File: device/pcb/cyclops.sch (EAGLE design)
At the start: 180 parts, among them Q1 SSM3K324, Q2 SSM3K324, Q3 SSM3K324, Q4 IRF510, U1 MCP4921, U10 ADG1202, U11 THS4281, U12 MAX4564, U13 ZXTD, U14 ZXTD, U15 OPA1664, U2 LT1931, U3 LT1764A, U31 TPS62153, U4 BD00FC0WEFJ, U5 TPS72325, U6 LT1711, U7 TLV3701, U8 ADR03, U9 LT1880

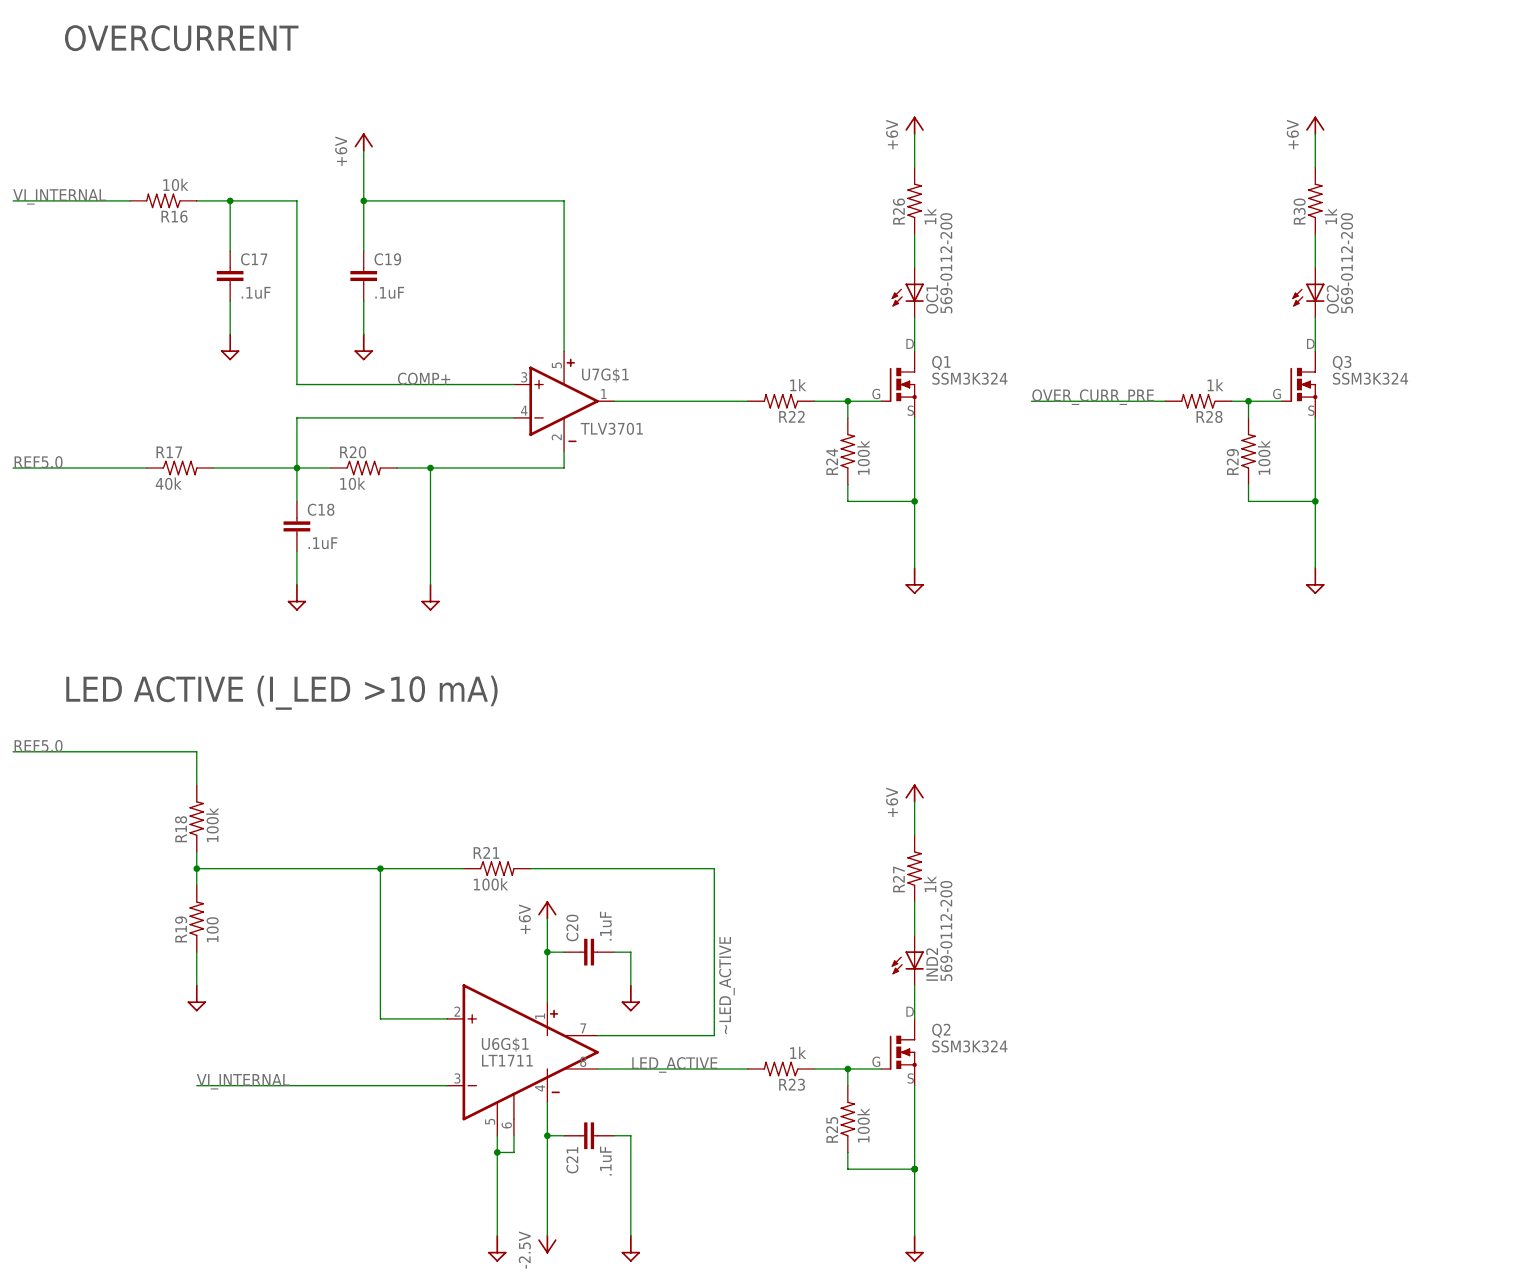
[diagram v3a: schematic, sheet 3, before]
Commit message: Minor circuit changes made during testing.
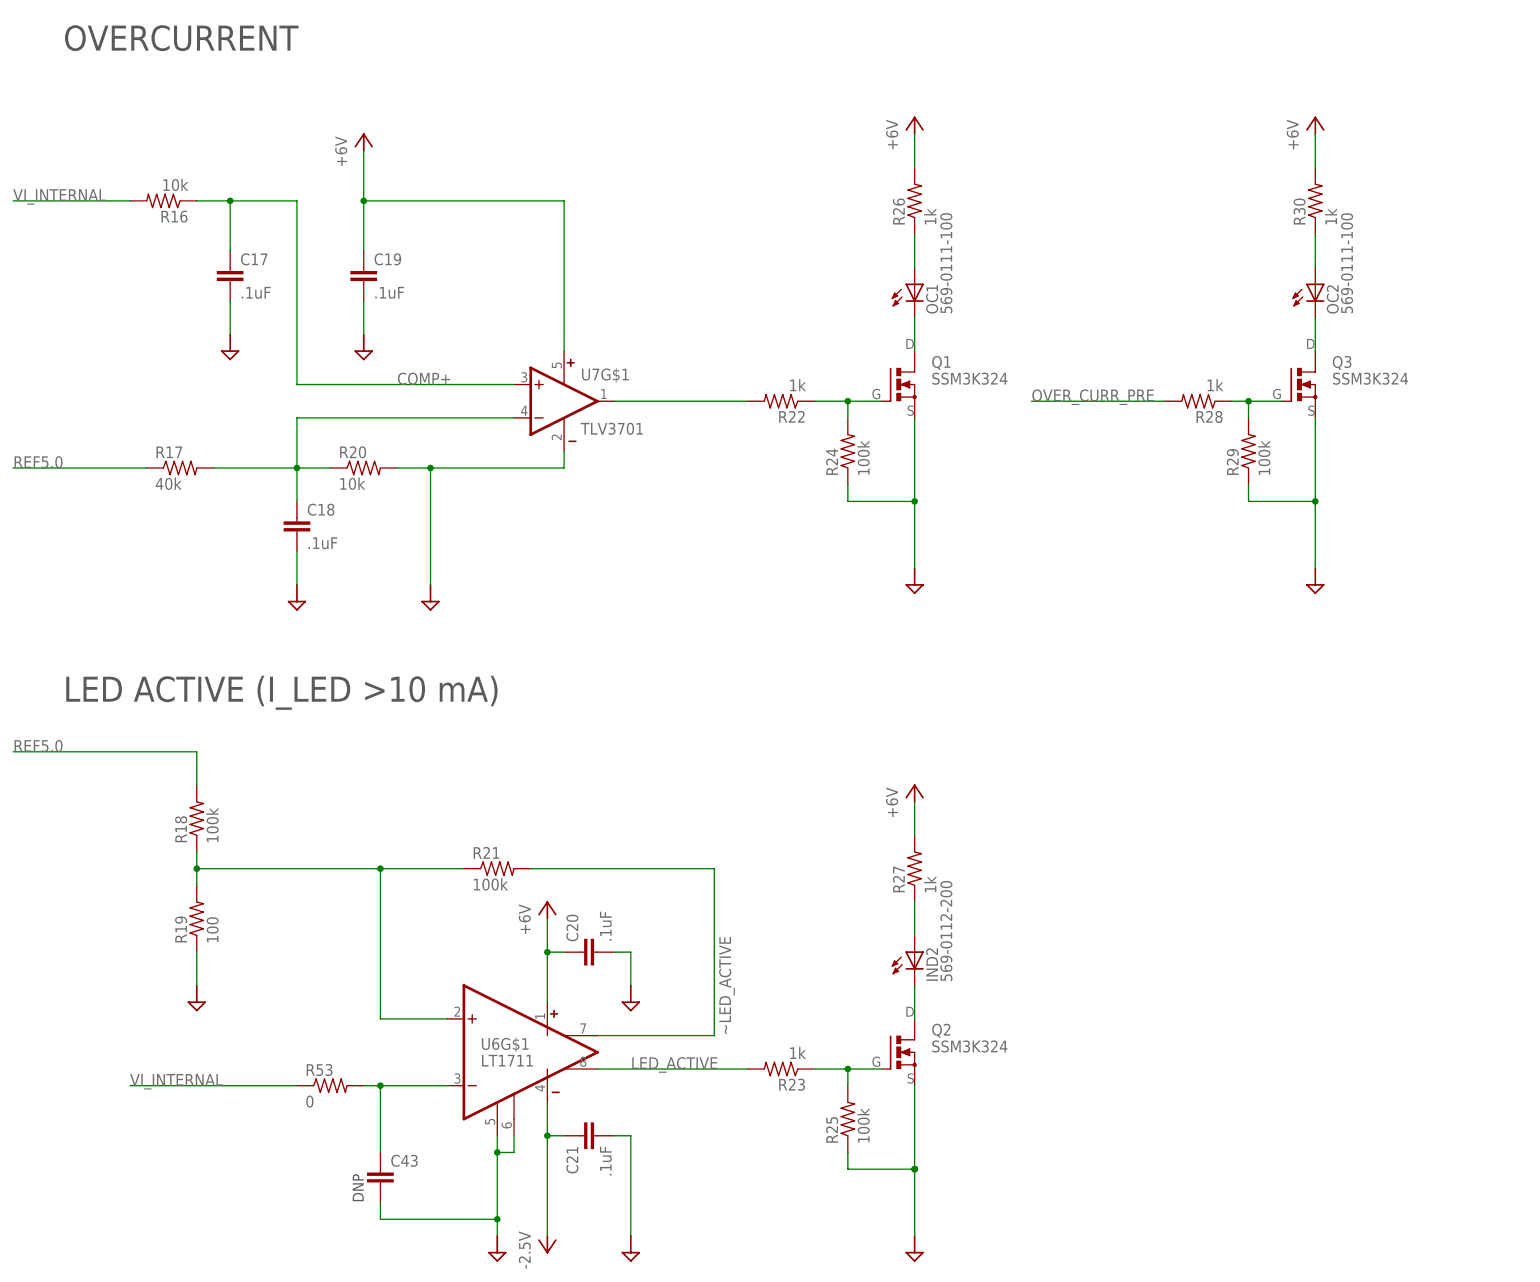
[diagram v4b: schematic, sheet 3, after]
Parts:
- added C43: (no value), cyclops:C_0603
- added R53: 0, cyclops:R_0603
- OC: value 569-0112-200 -> 569-0111-100
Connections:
- new net N$7: C43.1, R53.2, U6G$1.-IN
- net GND: now also C43.2
- net VI_INTERNAL: now also R53.1; no longer U6G$1.-IN
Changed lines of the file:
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@@
 <part name="R37" library="cyclops" deviceset="R" device="_0603" value="0"/>
 <part name="IND" library="jonnew" deviceset="LED_2X" device="_VERTICAL" value="569-0112-200"/>
-<part name="OC" library="jonnew" deviceset="LED_2X" device="_VERTICAL" value="569-0112-200"/>
+<part name="OC" library="jonnew" deviceset="LED_2X" device="_VERTICAL" value="569-0111-100"/>
 <part name="D2" library="jonnew" deviceset="S-DIODE" device="SOD-123" value="1N5819"/>
 <part name="VREF&lt;&gt;TTL" library="jonnew" deviceset="SPDT" device="_AS12A*" value="AS12CV"/>
@@
 <part name="U$80" library="jonnew" deviceset="TEENSY-2-PIN-HEADER" device="" value="PPPC021LFBN-RC"/>
 <part name="P+20" library="cyclops" deviceset="+5V" device="" value="+3V3"/>
+<part name="C43" library="cyclops" deviceset="C" device="_0603"/>
+<part name="R53" library="cyclops" deviceset="R" device="_0603" value="0"/>
 </parts>
 <sheets>
@@
 <text x="-109.22" y="22.86" size="3.81" layer="97">LED ACTIVE (I_LED &gt;10 mA)</text>
 <text x="-109.22" y="121.92" size="3.81" layer="97">OVERCURRENT</text>
+<text x="-63.5" y="-53.34" size="1.6764" layer="97" rot="R90">DNP</text>
 </plain>
 <instances>
@@
 <instance part="P+11" gate="1" x="20.32" y="10.16"/>
 <instance part="P+14" gate="1" x="-63.5" y="109.22"/>
+<instance part="C43" gate="C" x="-60.96" y="-48.26"/>
+<instance part="R53" gate="R" x="-68.58" y="-35.56" smashed="yes">
+<attribute name="NAME" x="-72.39" y="-34.0614" size="1.778" layer="95"/>
+<attribute name="VALUE" x="-72.39" y="-38.862" size="1.778" layer="96"/>
+</instance>
 </instances>
 <busses>
@@
 <wire x1="-43.18" y1="-45.72" x2="-43.18" y2="-43.18" width="0.1524" layer="91"/>
 <junction x="-43.18" y="-45.72"/>
-<wire x1="-43.18" y1="-45.72" x2="-43.18" y2="-58.42" width="0.1524" layer="91"/>
+<wire x1="-43.18" y1="-45.72" x2="-43.18" y2="-55.88" width="0.1524" layer="91"/>
+<pinref part="C43" gate="C" pin="2"/>
+<wire x1="-43.18" y1="-55.88" x2="-43.18" y2="-58.42" width="0.1524" layer="91"/>
+<wire x1="-60.96" y1="-53.34" x2="-60.96" y2="-55.88" width="0.1524" layer="91"/>
+<wire x1="-60.96" y1="-55.88" x2="-43.18" y2="-55.88" width="0.1524" layer="91"/>
+<junction x="-43.18" y="-55.88"/>
 </segment>
 <segment>
@@
 </segment>
 <segment>
-<label x="-88.9" y="-35.56" size="1.778" layer="95"/>
-<wire x1="-88.9" y1="-35.56" x2="-50.8" y2="-35.56" width="0.1524" layer="91"/>
-<pinref part="U6" gate="G$1" pin="-IN"/>
+<label x="-99.06" y="-35.56" size="1.778" layer="95"/>
+<pinref part="R53" gate="R" pin="1"/>
+<wire x1="-73.66" y1="-35.56" x2="-99.06" y2="-35.56" width="0.1524" layer="91"/>
 </segment>
 </net>
@@
 </segment>
 </net>
+<net name="N$7" class="0">
+<segment>
+<pinref part="R53" gate="R" pin="2"/>
+<pinref part="C43" gate="C" pin="1"/>
+<wire x1="-63.5" y1="-35.56" x2="-60.96" y2="-35.56" width="0.1524" layer="91"/>
+<wire x1="-60.96" y1="-35.56" x2="-60.96" y2="-45.72" width="0.1524" layer="91"/>
+<pinref part="U6" gate="G$1" pin="-IN"/>
+<wire x1="-60.96" y1="-35.56" x2="-50.8" y2="-35.56" width="0.1524" layer="91"/>
+<junction x="-60.96" y="-35.56"/>
+</segment>
+</net>

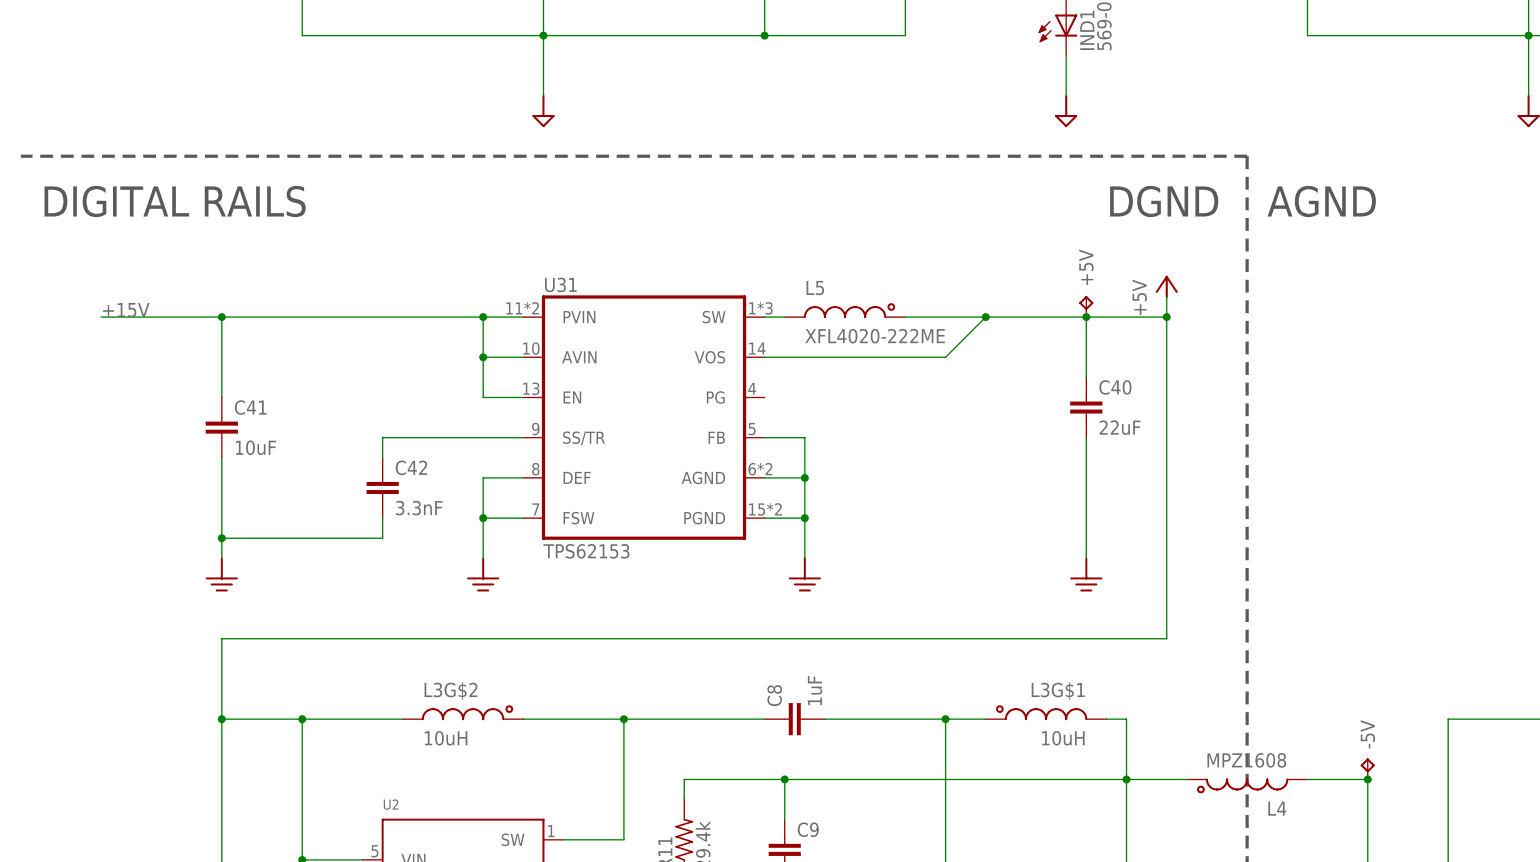
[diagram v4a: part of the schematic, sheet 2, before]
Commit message: Changes from benchtop testing 3.6
- Buck got replaced with LT uModule to reduce switching noise
- low pass filter input to LED on circuit to prevent glitching.
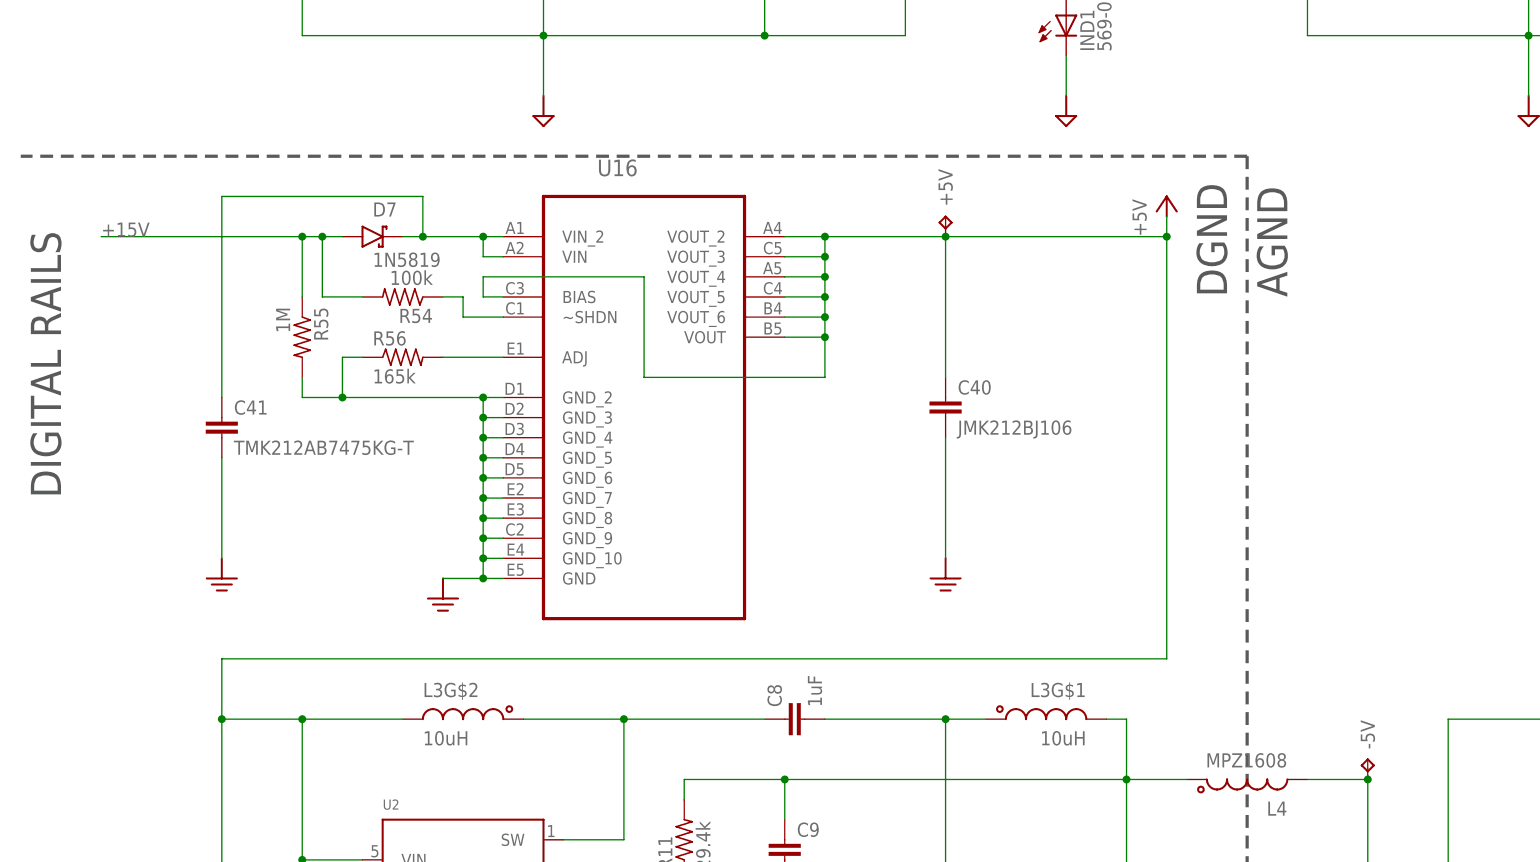
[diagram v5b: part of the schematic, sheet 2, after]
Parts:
- removed C42: 3.3nF, jonnew:C_0603
- removed L5: XFL4020-222ME, jonnew:L_4020
- removed U31: TPS62153, jonnew:TPS6125X_VQFN16
- added D7: 1N5819, jonnew:S-DIODESOD-123
- added R54: 100k, cyclops:R_0603
- added R55: 1M, cyclops:R_0603
- added R56: 165k, cyclops:R_0603
- added U16: (no value), jonnew:LTM8020IVPBF
- C40: value 22uF -> JMK212BJ106; device cyclops:C_1210 -> jonnew:C_0805
- C41: value 10uF -> TMK212AB7475KG-T; device jonnew:C_1206 -> jonnew:C_0805
- C43: value (none) -> 10nF
- R53: value 0 -> 100
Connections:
- removed net N$56: C42.1, U31.SS/TR
- removed net SW: L5.2, U31.SW
- new net N$21: C41.1, D7.C, U16.VIN, U16.VIN_2
- new net N$23: R54.1, U16.~SHDN
- new net N$38: R56.2, U16.ADJ
- net +15V: now also D7.A, R54.2, R55.1; no longer C41.1, U31.AVIN, U31.EN, U31.PVIN
- net +5V: now also U16.BIAS, U16.VOUT, U16.VOUT_2, U16.VOUT_3, U16.VOUT_4, U16.VOUT_5, U16.VOUT_6; no longer L5.1, U31.VOS
- net GND: now also R55.2, R56.1, U16.GND, U16.GND_10, U16.GND_2, U16.GND_3, U16.GND_4, U16.GND_5, U16.GND_6, U16.GND_7, U16.GND_8, U16.GND_9; no longer C42.2, U31.AGND, U31.DEF, U31.FB, U31.FSW, U31.PGND
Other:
- moved on the sheet: +5V, C40, C43

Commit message: Minor.
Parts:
- U10: value ADG1202 -> ADG1201
- U16: value (none) -> LTM8020
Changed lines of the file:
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@@
 <part name="P+1" library="jonnew" deviceset="+5V" device="" value="+6V"/>
 <part name="P+5" library="jonnew" deviceset="+5V" device="" value="+6V"/>
-<part name="U10" library="jonnew" deviceset="SPST_IC" device="_SOT23-6" value="ADG1202"/>
+<part name="U10" library="jonnew" deviceset="SPST_IC" device="_SOT23-6" value="ADG1201"/>
 <part name="P+9" library="jonnew" deviceset="+5V" device="" value="+6V"/>
 <part name="P+10" library="jonnew" deviceset="+5V" device="" value="+6V"/>
@@
 <part name="C43" library="cyclops" deviceset="C" device="_0603" value="10nF"/>
 <part name="R53" library="cyclops" deviceset="R" device="_0603" value="100"/>
-<part name="U16" library="jonnew" deviceset="LTM8020IVPBF" device=""/>
+<part name="U16" library="jonnew" deviceset="LTM8020IVPBF" device="" value="LTM8020"/>
 <part name="D7" library="jonnew" deviceset="S-DIODE" device="SOD-123" value="1N5819"/>
 <part name="R54" library="cyclops" deviceset="R" device="_0603" value="100k"/>
@@
 <wire x1="-2.54" y1="-27.94" x2="12.7" y2="-27.94" width="0.1524" layer="91"/>
 <pinref part="U16" gate="A" pin="BIAS"/>
-<wire x1="-43.18" y1="-35.56" x2="-45.72" y2="-35.56" width="0.1524" layer="91"/>
-<wire x1="-45.72" y1="-35.56" x2="-45.72" y2="-33.02" width="0.1524" layer="91"/>
-<wire x1="-45.72" y1="-33.02" x2="-25.4" y2="-33.02" width="0.1524" layer="91"/>
-<wire x1="-25.4" y1="-33.02" x2="-25.4" y2="-45.72" width="0.1524" layer="91"/>
-<wire x1="-25.4" y1="-45.72" x2="-2.54" y2="-45.72" width="0.1524" layer="91"/>
+<wire x1="-7.62" y1="-45.72" x2="-2.54" y2="-45.72" width="0.1524" layer="91"/>
 <wire x1="-2.54" y1="-45.72" x2="-2.54" y2="-40.64" width="0.1524" layer="91"/>
 <junction x="-2.54" y="-40.64"/>

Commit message: Towards final updates for revision 3.6
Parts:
- removed D1: 1N5819, jonnew:S-DIODESOD-123
- removed Q3: SSM3K324, jonnew:N-MOSFET_SOT23-GSD
- added U69: FDN352AP, jonnew:P-MOSFET_SOT23-GSD
- added VREF<>TTL1: AS12CV, jonnew:SPDT_AS12A*
- Q1, Q2: value SSM3K324 -> NDS351AN
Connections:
- net OVER_CURR_PRE renamed ~OVER_CURR_PRE
- removed net OC: OC2.C, Q3.D
- removed net OVER_CURR: U10.IN
- new net N$16: R30.2, U69.D
- new net N$19: VCTL.1, VREF<>TTL1.1
- net +6V: now also R29.1, U69.S; no longer R30.2
- net GND: now also OC2.C; no longer Q3.S, R29.1
- net N$39: now also U69.G; no longer Q3.G
- net REF5.0: now also VREF<>TTL1.3
- net VINPUT: now also VREF<>TTL1.2; no longer VCTL.1
- net ~OVER_CURR: now also U10.IN
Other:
- note added: "NOTE: 1N5818 S Diode and cut trace needed on the teensy to allow it to be powered both by USB and the Cyclops 5V rail."
- moved on the sheet: OC2, R28, R29, R30, VCTL
